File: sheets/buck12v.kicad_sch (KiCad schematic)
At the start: 11 parts, among them U1 LM2575-12BU

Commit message: add MCU + output
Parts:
- renumbered R3 to R1, R1 to R2, R2 to R3
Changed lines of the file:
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@@
 		(dnp no)
 		(fields_autoplaced yes)
-		(property "Reference" "R3"
+		(property "Reference" "R1"
 			(at 166.37 87.6299 0)
 			(effects
@@
 			(project "esp32-didatic-kit"
 				(path "/f57920a5-fee7-4fe5-a133-e8b36941a5a6/68eb6d36-2b61-4a79-8b9e-43cc2ec0c3c5/a4fbb455-48dc-4e33-aa46-f1d410f99810"
-					(reference "R3")
+					(reference "R1")
 					(unit 1)
 				)
@@
 		(dnp no)
 		(fields_autoplaced yes)
-		(property "Reference" "R1"
+		(property "Reference" "R2"
 			(at 170.18 66.04 90)
 			(effects
@@
 			(project ""
 				(path "/f57920a5-fee7-4fe5-a133-e8b36941a5a6/68eb6d36-2b61-4a79-8b9e-43cc2ec0c3c5/a4fbb455-48dc-4e33-aa46-f1d410f99810"
-					(reference "R1")
+					(reference "R2")
 					(unit 1)
 				)
@@
 		(dnp no)
 		(fields_autoplaced yes)
-		(property "Reference" "#PWR02"
+		(property "Reference" "#PWR09"
 			(at 66.04 116.84 0)
 			(effects
@@
 			(project ""
 				(path "/f57920a5-fee7-4fe5-a133-e8b36941a5a6/68eb6d36-2b61-4a79-8b9e-43cc2ec0c3c5/a4fbb455-48dc-4e33-aa46-f1d410f99810"
-					(reference "#PWR02")
+					(reference "#PWR09")
 					(unit 1)
 				)
@@
 		(dnp no)
 		(fields_autoplaced yes)
-		(property "Reference" "R2"
+		(property "Reference" "R3"
 			(at 180.34 66.7097 90)
 			(effects
@@
 			(project ""
 				(path "/f57920a5-fee7-4fe5-a133-e8b36941a5a6/68eb6d36-2b61-4a79-8b9e-43cc2ec0c3c5/a4fbb455-48dc-4e33-aa46-f1d410f99810"
-					(reference "R2")
-					(unit 1)
-				)
+					(reference "R3")
+					(unit 1)
+				)

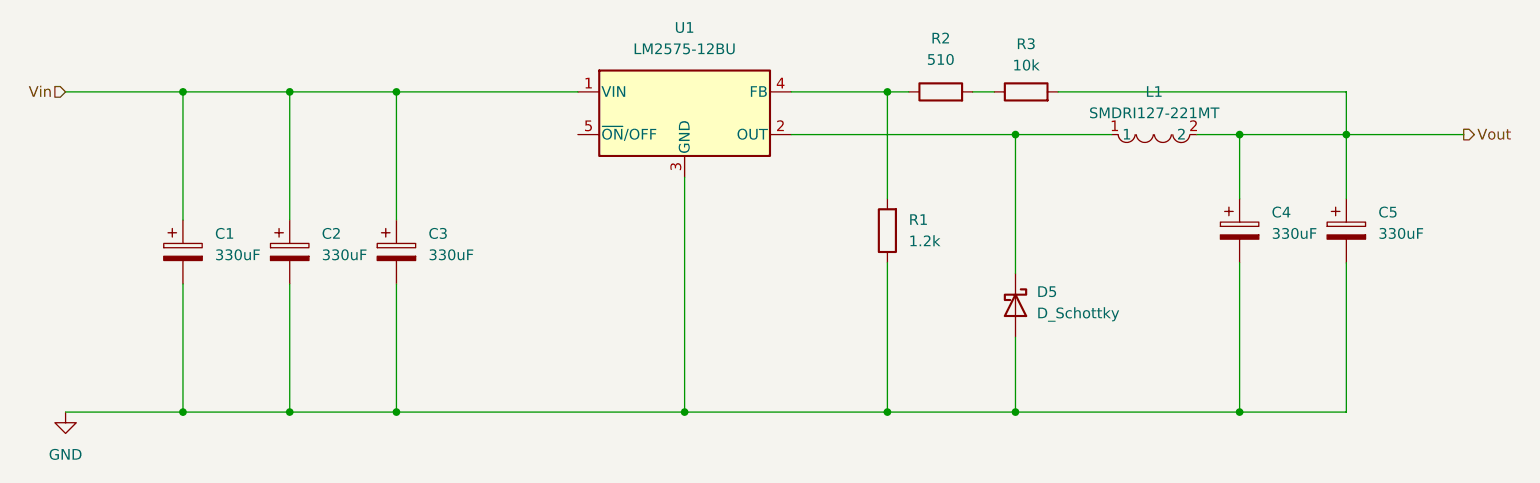
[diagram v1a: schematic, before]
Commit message: Updated MCU to MCU module + set SMD comp. footprints
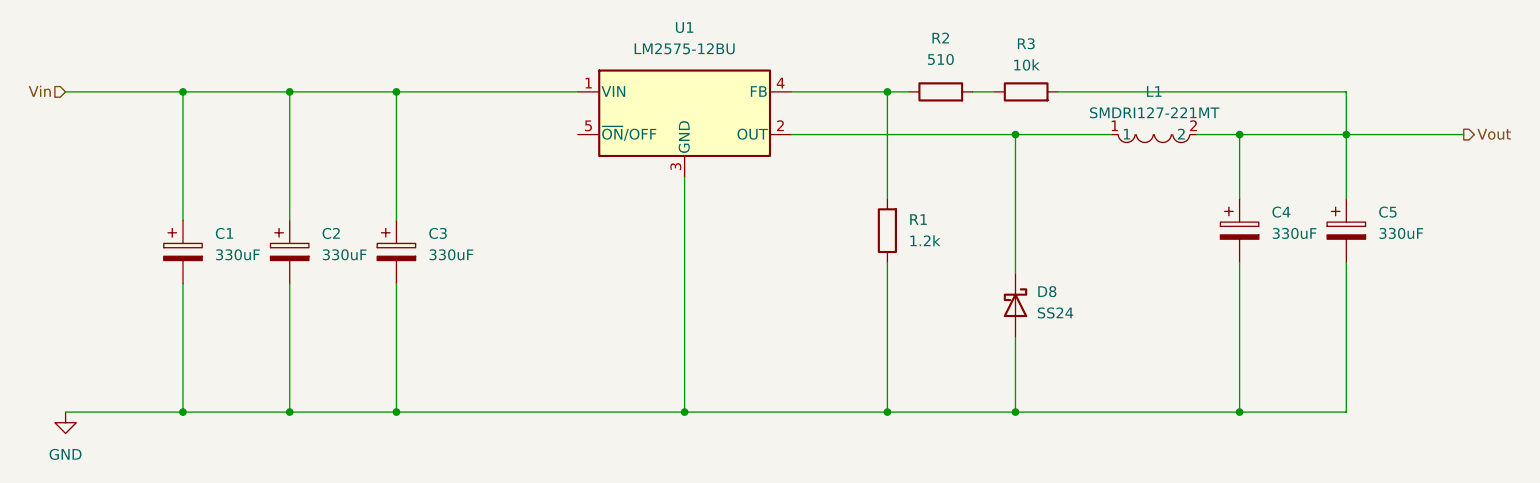
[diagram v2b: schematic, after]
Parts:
- removed D5: D_Schottky, symbol Device:D_Schottky
- added D8: SS24, Diode_SMD:D_SMA, symbol Diode:SS24
- R1, R2, R3: footprint (none) -> Resistor_SMD:R_0603_1608Metric
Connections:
- net GND: now also D8.2 (A)
- net at L1.1, U1.2 (OUT): now also D8.1 (K)
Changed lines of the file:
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@@
-	)
-	(symbol
-		(lib_id "Device:D_Schottky")
-		(at 179.07 97.79 270)
-		(unit 1)
-		(exclude_from_sim no)
-		(in_bom yes)
-		(on_board yes)
-		(dnp no)
-		(fields_autoplaced yes)
-		(property "Reference" "D5"
-			(at 181.61 96.2024 90)
-			(effects
-				(font
-					(size 1.27 1.27)
-				)
-				(justify left)
-			)
-		)
-		(property "Value" "D_Schottky"
-			(at 181.61 98.7424 90)
-			(effects
-				(font
-					(size 1.27 1.27)
-				)
-				(justify left)
-			)
-		)
-		(property "Footprint" ""
-			(at 179.07 97.79 0)
-			(effects
-				(font
-					(size 1.27 1.27)
-				)
-				(hide yes)
-			)
-		)
-		(property "Datasheet" "~"
-			(at 179.07 97.79 0)
-			(effects
-				(font
-					(size 1.27 1.27)
-				)
-				(hide yes)
-			)
-		)
-		(property "Description" "Schottky diode"
-			(at 179.07 97.79 0)
-			(effects
-				(font
-					(size 1.27 1.27)
-				)
-				(hide yes)
-			)
-		)
-		(pin "2"
-		)
-		(pin "1"
-		)
-		(instances
-			(project ""
-				(path "/f57920a5-fee7-4fe5-a133-e8b36941a5a6/68eb6d36-2b61-4a79-8b9e-43cc2ec0c3c5/a4fbb455-48dc-4e33-aa46-f1d410f99810"
-					(reference "D5")
-					(unit 1)
-				)
-			)
-		)
 	)
 	(symbol
@@
 			)
 		)
-		(property "Footprint" ""
+		(property "Footprint" "Resistor_SMD:R_0603_1608Metric"
 			(at 165.608 88.9 90)
 			(effects
@@
 			)
 		)
-		(property "Footprint" ""
+		(property "Footprint" "Resistor_SMD:R_0603_1608Metric"
 			(at 170.18 74.168 90)
 			(effects
@@
 	)
 	(symbol
+		(lib_id "Diode:SS24")
+		(at 179.07 97.79 270)
+		(unit 1)
+		(exclude_from_sim no)
+		(in_bom yes)
+		(on_board yes)
+		(dnp no)
+		(fields_autoplaced yes)
+		(property "Reference" "D8"
+			(at 181.61 96.2024 90)
+			(effects
+				(font
+					(size 1.27 1.27)
+				)
+				(justify left)
+			)
+		)
+		(property "Value" "SS24"
+			(at 181.61 98.7424 90)
+			(effects
+				(font
+					(size 1.27 1.27)
+				)
+				(justify left)
+			)
+		)
+		(property "Footprint" "Diode_SMD:D_SMA"
+			(at 174.625 97.79 0)
+			(effects
+				(font
+					(size 1.27 1.27)
+				)
+				(hide yes)
+			)
+		)
+		(property "Datasheet" "https://www.vishay.com/docs/88748/ss22.pdf"
+			(at 179.07 97.79 0)
+			(effects
+				(font
+					(size 1.27 1.27)
+				)
+				(hide yes)
+			)
+		)
+		(property "Description" "40V 2A Schottky Diode, SMA"
+			(at 179.07 97.79 0)
+			(effects
+				(font
+					(size 1.27 1.27)
+				)
+				(hide yes)
+			)
+		)
+		(pin "1"
+		)
+		(pin "2"
+		)
+		(instances
+			(project ""
+				(path "/f57920a5-fee7-4fe5-a133-e8b36941a5a6/68eb6d36-2b61-4a79-8b9e-43cc2ec0c3c5/a4fbb455-48dc-4e33-aa46-f1d410f99810"
+					(reference "D8")
+					(unit 1)
+				)
+			)
+		)
+	)
+	(symbol
 		(lib_id "Device:C_Polarized")
 		(at 218.44 88.9 0)
@@
 			)
 		)
-		(property "Footprint" ""
+		(property "Footprint" "Resistor_SMD:R_0603_1608Metric"
 			(at 180.34 74.168 90)
 			(effects
